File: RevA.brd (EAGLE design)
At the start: 106 x 53 mm, 61 parts, among them IC1 MAX31855, IC10 DS3231/SO, IC3 MAX31855, IC4 MAX31855, IC5 MAX31855, IC9 ATMEGA32U4-AU, J1 1X2-3.5MM, J2 1X2-3.5MM, J3 1X2-3.5MM, J4 1X2-3.5MM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

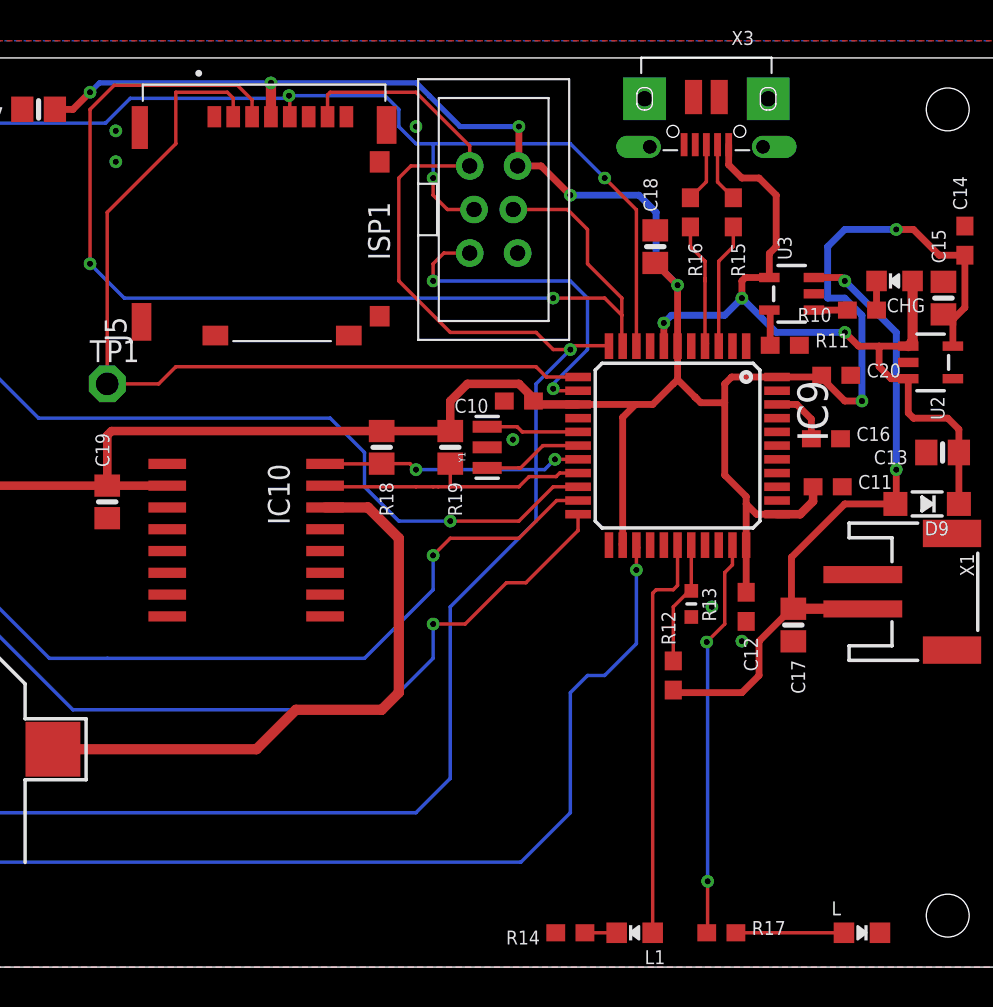
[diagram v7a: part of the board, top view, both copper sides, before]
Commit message: Removed crossovers in traces
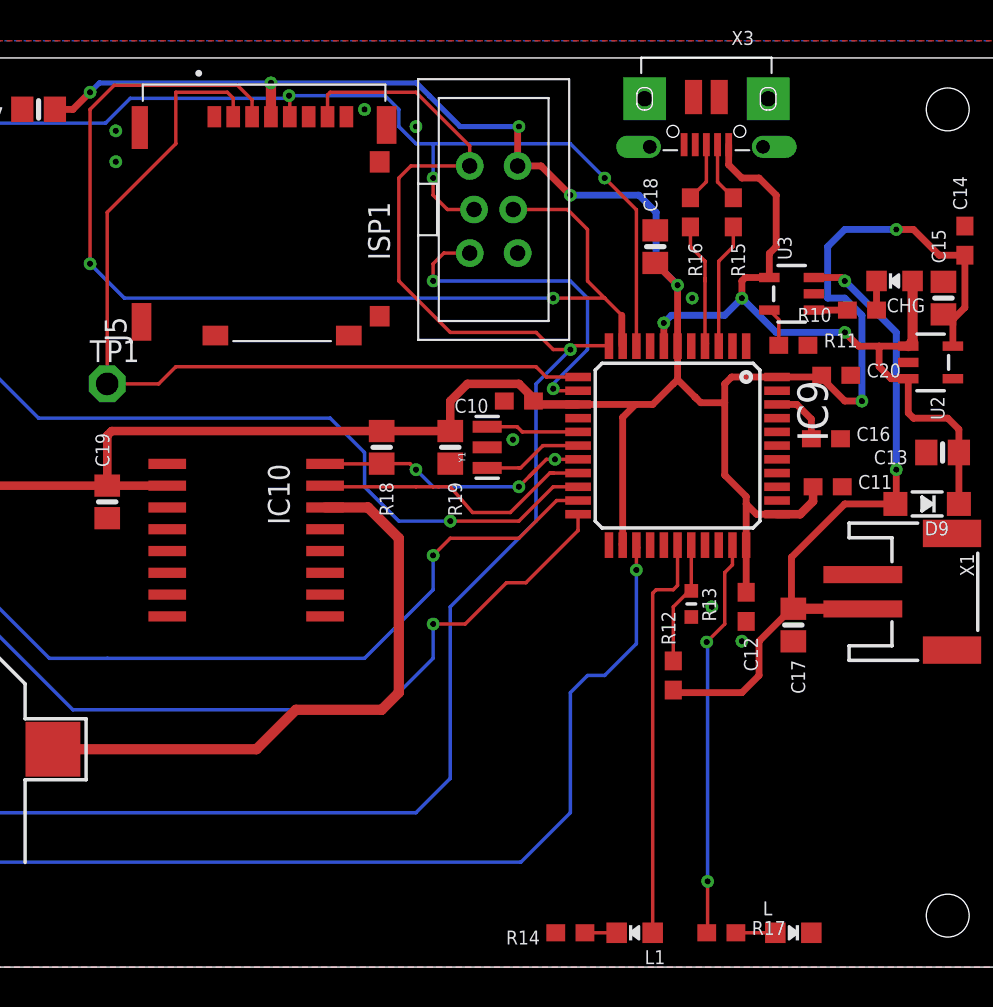
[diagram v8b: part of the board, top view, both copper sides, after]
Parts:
- moved L 4.00 mm to (94.0, 2.00)
- moved R11 0.50 mm to (94.0, 36.2)
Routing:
- net N$33: track 6.32 -> 2.32 mm
- net MOSI: track 65.1 -> 63.7 mm
- net SCL: track 15.1 -> 16.5 mm, vias 2 -> 3
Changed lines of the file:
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@@
 <layer number="20" name="Dimension" color="24" fill="1" visible="yes" active="yes"/>
 <layer number="21" name="tPlace" color="7" fill="1" visible="yes" active="yes"/>
-<layer number="22" name="bPlace" color="7" fill="1" visible="yes" active="yes"/>
+<layer number="22" name="bPlace" color="7" fill="1" visible="no" active="yes"/>
 <layer number="23" name="tOrigins" color="15" fill="1" visible="yes" active="yes"/>
-<layer number="24" name="bOrigins" color="15" fill="1" visible="yes" active="yes"/>
+<layer number="24" name="bOrigins" color="15" fill="1" visible="no" active="yes"/>
 <layer number="25" name="tNames" color="7" fill="1" visible="yes" active="yes"/>
 <layer number="26" name="bNames" color="7" fill="1" visible="no" active="yes"/>
@@
 </layers>
 <board>
-<fusionsync huburn="a.cGVyc29uYWw6dWUyYmRkYjQx" projecturn="a.cGVyc29uYWw6dWUyYmRkYjQxIzIwMTgwNTAyMTMwMjU4MzAx" f3durn="urn:adsk.wipprod:dm.lineage:a68wfmUxQy2LyGLi9FcYGg" pcbguid="62a8e096-691a-4df0-bd8f-1dbb8bf064d3" lastpulledtime="" lastsyncedchangeguid="eced6e01-4855-4ae4-9f9e-6e16df8c0a8d"/>
+<fusionsync huburn="a.cGVyc29uYWw6dWUyYmRkYjQx" projecturn="a.cGVyc29uYWw6dWUyYmRkYjQxIzIwMTgwNTAyMTMwMjU4MzAx" f3durn="urn:adsk.wipprod:dm.lineage:a68wfmUxQy2LyGLi9FcYGg" pcbguid="62a8e096-691a-4df0-bd8f-1dbb8bf064d3" lastpulledtime="" lastsyncedchangeguid="943978a0-c9d0-5ed7-44f3-79418516dc5a"/>
 <plain>
 <wire x1="0" y1="0" x2="106" y2="0" width="0" layer="20"/>
@@
 <element name="IC9" library="microbuilder" package="TQFP44" value="ATMEGA32U4-AU" x="87.25" y="30.4" rot="R270"/>
 <element name="J1" library="adafruit" package="1X2-3.5MM" value="1X2-3.5MM" x="5.5" y="45.3" rot="R270"/>
-<element name="L" library="microbuilder" package="CHIPLED_0805_NOOUTLINE" value="RED" x="98" y="2" rot="R270"/>
+<element name="L" library="microbuilder" package="CHIPLED_0805_NOOUTLINE" value="RED" x="94" y="2" rot="R270"/>
 <element name="L1" library="microbuilder" package="CHIPLED_0805_NOOUTLINE" value="GREEN" x="84.75" y="2" rot="R90"/>
 <element name="R10" library="microbuilder" package="0603-NO" value="1K" x="98" y="38.3" rot="R180"/>
-<element name="R11" library="microbuilder" package="0603-NO" value="10K\" x="93.5" y="36.25"/>
+<element name="R11" library="microbuilder" package="0603-NO" value="10K\" x="94" y="36.25"/>
 <element name="R12" library="microbuilder" package="0603-NO" value="100k" x="87" y="17" rot="R90"/>
 <element name="R13" library="microbuilder" package="_0603MP" value="100K" x="88.05" y="21.17" rot="R270"/>
@@
 </elements>
 <signals>
-<signal name="GND">
+<signal name="GND" airwireshidden="yes">
 <contactref element="C1" pad="2"/>
 <contactref element="C2" pad="2"/>
@@
 <via x="54.5" y="46.95" extent="1-16" drill="0.35"/>
 <via x="72" y="49" extent="1-16" drill="0.35"/>
+<via x="69" y="50" extent="1-16" drill="0.35"/>
+<via x="88.1" y="39" extent="1-16" drill="0.35"/>
 <wire x1="92.23" y1="47.82" x2="92.53" y2="50.62" width="0" layer="19" extent="1-1"/>
 <wire x1="85.33" y1="50.62" x2="85.63" y2="47.82" width="0" layer="19" extent="1-1"/>
 <wire x1="88.18" y1="50.72" x2="87.63" y2="47.945" width="0" layer="19" extent="1-1"/>
-<wire x1="70.2898" y1="49.092" x2="65.7448" y2="49.572" width="0" layer="19" extent="1-1"/>
 </signal>
 <signal name="CS-1">
@@
 <via x="81" y="45" extent="1-16" drill="0.35"/>
 <wire x1="81" y1="45" x2="79.296" y2="46.704" width="0.4" layer="1"/>
-<wire x1="79.296" y1="46.704" x2="78" y2="46.704" width="0.4" layer="1"/>
 <wire x1="63.5448" y1="49.572" x2="63.5448" y2="51.5448" width="0.6" layer="1"/>
 <via x="63.5448" y="51.5448" extent="1-16" drill="0.35"/>
@@
 <wire x1="74.5747375" y1="49" x2="78" y2="49" width="0.3" layer="16"/>
 <wire x1="72.78736875" y1="50.78736875" x2="74.5747375" y2="49" width="0.3" layer="16"/>
-<wire x1="78" y1="49" x2="78" y2="46.704" width="0.4" layer="1"/>
 <wire x1="54" y1="28.07" x2="54.005" y2="28.065" width="0.2032" layer="1"/>
 <wire x1="20" y1="41" x2="22" y2="41" width="0.6" layer="1"/>
@@
 <wire x1="54" y1="28.07" x2="53.995" y2="28.065" width="0.5" layer="1"/>
 <wire x1="53.995" y1="28.065" x2="47.065" y2="28.065" width="0.5" layer="1"/>
-<wire x1="54.25" y1="31.25" x2="54" y2="31" width="0.5" layer="1"/>
 <wire x1="54.005" y1="30.995" x2="54.005" y2="28.065" width="0.5" layer="1"/>
-<wire x1="70" y1="31.25" x2="54.25" y2="31.25" width="0.5" layer="1"/>
 <wire x1="87.25" y1="36.2" x2="87.25" y2="39.75" width="0.4" layer="1"/>
 <via x="87.25" y="39.75" extent="1-16" drill="0.35"/>
@@
 <wire x1="88.6" y1="32.9" x2="90" y2="32.9" width="0.4" layer="1"/>
 <wire x1="93.05" y1="34.4" x2="95.55" y2="34.4" width="0.4" layer="1"/>
-<wire x1="78" y1="46.704" x2="77.9266" y2="46.704" width="0" layer="19" extent="1-1"/>
-<wire x1="54.005" y1="30.995" x2="54" y2="31" width="0" layer="19" extent="1-1"/>
+<wire x1="70" y1="31.25" x2="54.26" y2="31.25" width="0.5" layer="1"/>
+<wire x1="54.26" y1="31.25" x2="54.005" y2="30.995" width="0.5" layer="1"/>
+<wire x1="79.296" y1="46.704" x2="77.9266" y2="46.704" width="0.4" layer="1"/>
+<wire x1="78" y1="49" x2="77.9266" y2="48.9266" width="0.4" layer="1"/>
+<wire x1="77.9266" y1="48.9266" x2="77.9266" y2="46.704" width="0.4" layer="1"/>
 </signal>
 <signal name="SCK">
@@
 <contactref element="R11" pad="1"/>
 <wire x1="92.5999" y1="38.3" x2="92.65" y2="38.2499" width="0.4" layer="1"/>
-<wire x1="92.65" y1="38.2499" x2="92.65" y2="36.25" width="0.4" layer="1"/>
+<wire x1="92.5999" y1="38.3" x2="93.15" y2="37.7499" width="0.2032" layer="1"/>
+<wire x1="93.15" y1="37.7499" x2="93.15" y2="36.25" width="0.2032" layer="1"/>
 </signal>
 <signal name="MOSI">
@@
 <via x="80" y="39" extent="1-16" drill="0.35"/>
 <wire x1="84.05" y1="36.2" x2="84" y2="36.25" width="0.2032" layer="1"/>
-<wire x1="84" y1="36.25" x2="84" y2="38" width="0.2032" layer="1"/>
-<wire x1="84" y1="39" x2="84" y2="38" width="0.2032" layer="1"/>
+<wire x1="84" y1="36.25" x2="84" y2="38" width="0.4" layer="1"/>
 <wire x1="80" y1="39" x2="83" y2="39" width="0.2032" layer="1"/>
 <wire x1="83" y1="39" x2="84" y2="38" width="0.2032" layer="1"/>
-<wire x1="82" y1="43" x2="82" y2="41" width="0.2032" layer="1"/>
-<wire x1="82" y1="41" x2="84" y2="39" width="0.2032" layer="1"/>
 <wire x1="53" y1="50" x2="53" y2="41" width="0.2032" layer="1"/>
 <via x="53" y="41" extent="1-16" drill="0.35"/>
@@
 <wire x1="55" y1="39" x2="80" y2="39" width="0.2032" layer="16"/>
 <wire x1="77.6726" y1="44.164" x2="80.836" y2="44.164" width="0.2032" layer="1"/>
+<wire x1="82" y1="40" x2="83" y2="39" width="0.2032" layer="1"/>
+<wire x1="82" y1="43" x2="82" y2="40" width="0.2032" layer="1"/>
 </signal>
 <signal name="MISO">
@@
 <contactref element="R17" pad="2"/>
 <wire x1="90.65" y1="2" x2="90.67" y2="2" width="0.2032" layer="1"/>
-<wire x1="90.65" y1="2" x2="96.95" y2="2" width="0.2032" layer="1"/>
+<wire x1="90.65" y1="2" x2="92.95" y2="2" width="0.2032" layer="1"/>
 </signal>
 <signal name="SDA">
@@
 <wire x1="66.765" y1="28" x2="72" y2="28" width="0.2032" layer="1"/>
 <wire x1="74" y1="29" x2="74" y2="29.35" width="0.2032" layer="1"/>
-<wire x1="81.45" y1="28.8" x2="80.3747375" y2="28.8" width="0.2032" layer="1"/>
-<wire x1="80.3747375" y1="28.8" x2="80.1683375" y2="28.5936" width="0.2032" layer="1"/>
-<wire x1="78.5936" y1="28.5936" x2="80.1683375" y2="28.5936" width="0.2032" layer="1"/>
 <wire x1="73" y1="28" x2="73" y2="28" width="0.2032" layer="1"/>
-<wire x1="78" y1="28" x2="78.5936" y2="28.5936" width="0.2032" layer="1"/>
 <wire x1="73" y1="28" x2="73.3" y2="28" width="0.2032" layer="1"/>
 <wire x1="73.3" y1="28" x2="74" y2="28" width="0.2032" layer="1"/>
-<wire x1="74" y1="28" x2="78" y2="28" width="0.2032" layer="1"/>
 <wire x1="74" y1="29.35" x2="73.65" y2="29" width="0.2032" layer="1"/>
-<wire x1="74" y1="29.35" x2="74" y2="28" width="0.2032" layer="1"/>
+<wire x1="79.8" y1="28.8" x2="80" y2="28.8" width="0.2032" layer="1"/>
+<wire x1="80" y1="28.8" x2="81.45" y2="28.8" width="0.2032" layer="1"/>
+<wire x1="74" y1="28" x2="75.3" y2="26.5" width="0.2032" layer="1"/>
+<wire x1="75.3" y1="26.5" x2="77.5" y2="26.5" width="0.2032" layer="1"/>
+<wire x1="79.8" y1="28.8" x2="80" y2="28.8" width="0.2032" layer="1"/>
+<wire x1="77.5" y1="26.5" x2="79.8" y2="28.8" width="0.2032" layer="1"/>
+<wire x1="74" y1="28" x2="74" y2="29" width="0" layer="19" extent="1-1"/>
 </signal>
 <signal name="SCL">
@@
 <wire x1="81.45" y1="29.6" x2="80.1" y2="29.6" width="0.2032" layer="1"/>
 <via x="80.1" y="29.6" extent="1-16" drill="0.35"/>
-<wire x1="80.1" y1="29.6" x2="79.5" y2="29" width="0.2032" layer="16"/>
-<wire x1="79.5" y1="29" x2="72" y2="29" width="0.2032" layer="16"/>
+<wire x1="80.1" y1="29.6" x2="79.6" y2="29.6" width="0.2032" layer="1"/>
+<wire x1="79.6" y1="29.6" x2="79" y2="29" width="0.2032" layer="1"/>
+<wire x1="79" y1="29" x2="78.6" y2="28.6" width="0.2032" layer="1"/>
+<wire x1="79" y1="29" x2="78" y2="28" width="0.2032" layer="1"/>
+<via x="78" y="28" extent="1-16" drill="0.35"/>
+<wire x1="78" y1="28" x2="73" y2="28" width="0.2032" layer="16"/>
+<wire x1="73" y1="28" x2="72" y2="29" width="0.2032" layer="16"/>
 </signal>
 <signal name="32KHZ">
